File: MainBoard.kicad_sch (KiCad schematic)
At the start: 85 parts, among them J1 Conn_01x04, J10 Conn_01x02, J11 Conn_01x03, J12 Conn_01x03, J13 Conn_01x04, J14 Conn_01x03, J15 Conn_01x04, J16 Conn_01x05, J17 Conn_01x05, J18 Conn_01x06, J19 Conn_01x05, J2 Conn_01x04, J20 Conn_01x08, J21 Conn_01x03, J22 Conn_01x03, J23 Conn_01x05, J24 Conn_01x04, J25 Conn_01x04, J26 Conn_01x04, J27 Conn_01x04, J28 Conn_01x04, J3 Conn_01x06, J4 Conn_01x02, J5 Conn_01x02, J6 Conn_01x02, J7 Conn_01x04, J8 Conn_01x04, J9 Conn_01x02, Q1 NMOS_80A, Q10 NMOS_80A, Q11 NMOS_80A, Q12 NMOS, Q2 NMOS_80A, Q3 NMOS_80A, Q4 NMOS, Q5 NMOS, Q6 NMOS, Q7 NMOS, Q8 NMOS, Q9 NMOS, U1 TJA1051T-3, U10 INA228, U2 INA228, U5 INA228, U6 ESP32-DEVKITC-32D, U7 MCP23017_SO, U8 MCP23017_SO, U9 INA228

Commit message: test
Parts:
- removed C1, C2, C3, C4, C5, C6: 100nF, Capacitor_SMD:C_1206_3216Metric_Pad1.33x1.80mm_HandSolder, symbol Device:C
- removed D1, D2, D3, D4, D8, D9: US1M, Diode_SMD:D_SMA, symbol Diode:US1M
- removed D10, D11, D5, D6, D7: WS2812B, LED_SMD:LED_WS2812B_PLCC4_5.0x5.0mm_P3.2mm, symbol LED:WS2812B
- removed J1, J13, J15, J2, J24, J25, J26, J27, J28, J7, J8: Conn_01x04, velion_mainboard:15EDG-4P, symbol Connector_Generic:Conn_01x04
- removed J10, J4, J5, J6, J9: Conn_01x02, velion_mainboard:15EDG-2P, symbol Connector_Generic:Conn_01x02
- removed J11, J12, J14, J21, J22: Conn_01x03, velion_mainboard:15EDG-3P, symbol Connector_Generic:Conn_01x03
- removed J16, J17, J19, J23: Conn_01x05, velion_mainboard:15EDG-5P, symbol Connector_Generic:Conn_01x05
- removed J18, J3: Conn_01x06, velion_mainboard:15EDG-6P, symbol Connector_Generic:Conn_01x06
- removed J20: Conn_01x08, velion_mainboard:GY-91, symbol Connector_Generic:Conn_01x08
- removed Q1, Q10, Q11, Q2, Q3: NMOS_80A, velion_mainboard:NMOS_80A, symbol Transistor_FET_Other:Q_NMOS_Depletion_GDS
- removed Q12, Q4, Q5, Q6, Q7, Q8, Q9: NMOS, Package_TO_SOT_SMD:SOT-23, symbol Transistor_FET_Other:Q_NMOS_Depletion_GSD
- removed R1, R2, R8, R9: 0.001 R, Resistor_SMD:R_2512_6332Metric_Pad1.40x3.35mm_HandSolder, symbol Device:R
- removed R10, R12, R13, R14, R15, R16: 100 R, Resistor_SMD:R_1206_3216Metric_Pad1.30x1.75mm_HandSolder, symbol Device:R
- removed R11, R17: 10 K, Resistor_SMD:R_1206_3216Metric_Pad1.30x1.75mm_HandSolder, symbol Device:R
- removed R18: 120 R, Resistor_SMD:R_1206_3216Metric_Pad1.30x1.75mm_HandSolder, symbol Device:R
- removed R3, R4, R5: 100R, Resistor_SMD:R_1206_3216Metric_Pad1.30x1.75mm_HandSolder, symbol Device:R
- removed R6, R7: 4k7, Resistor_SMD:R_1206_3216Metric_Pad1.30x1.75mm_HandSolder, symbol Device:R
- removed U1: TJA1051T-3, Package_SO:SOIC-8_3.9x4.9mm_P1.27mm, symbol Interface_CAN_LIN:TJA1051T-3
- removed U10, U2, U5, U9: INA228, Package_SO:VSSOP-10_3x3mm_P0.5mm, symbol Sensor_Energy:INA228
- removed U3: ~, velion_mainboard:BUCK5V, symbol velion_mainboard:buck5V
- removed U4: ~, velion_mainboard:BUCK12V, symbol velion_mainboard:buck12V
- removed U6: ESP32-DEVKITC-32D, velion_mainboard:MODULE_ESP32-DEVKITC-32D, symbol ESP32-DEVKITC-32D:ESP32-DEVKITC-32D
- removed U7, U8: MCP23017_SO, Package_SO:SOIC-28W_7.5x17.9mm_P1.27mm, symbol Interface_Expansion:MCP23017_SO
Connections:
- no-connect marks 22 -> 0
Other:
- note added: "test"
- note removed: "(3V3-2V)/10 mA=100 R"
- note removed: "+ - -"
- note removed: "0100000 = 0x20"
- note removed: "0100001 = 0x21"
- note removed: "1 mosfet 40 A 1 mosfet 10 A 9 mosfet 5 A 1 current sensing 40 A 1 current sensing 10 A 4 current sensing 5 A 9 IO for 3 rotatary encoder (A/B + button) 2 IO for PAS 1 IO for Speed Input 2 IO brake sensor switch 1 IO seat sensor switch 1 IO trunk latch switch 5 IO LED 2 IO reverse selector 1 IO defrost button 1 IO cabin light button 1 IO warning button 1 IO brouillard button 1 IO WS2812"
- note removed: "1-2 CHF N-channel 100V 0.012 Ohm 80A"
- note removed: "1000000 -> 0x40"
- note removed: "1000001 -> 0x41"
- note removed: "1000100 -> 0x44"
- note removed: "1000101 -> 0x45"
- note removed: "10A"
- note removed: "10A Fuse here"
- note removed: "2A MAX"
- note removed: "2A max"
- note removed: "35-60V"
- note removed: "3v3 provided by internal LDO of ESP32 devboard"
- note removed: "40A Fuse Here"
- note removed: "40A Fuse here"
- note removed: "5 V"
- note removed: "5-12 V"
- note removed: "5A MAX"
- note removed: "AUX Power distribution"
- note removed: "AUX USB-C"
- note removed: "AUX audio"
- note removed: "Blinker + Trunk Latch + Int light"
- note removed: "Brouillard button + led"
- note removed: "Buttons Dashboard"
- note removed: "CAN BUS Power Rail"
- note removed: "CAN Display"
- note removed: "CAN Front"
- note removed: "CAN Handle"
- note removed: "CAN REAR"
- note removed: "CAN Transceiver"
- note removed: "CabinLighting button + led"
- note removed: "Compute"
- note removed: "Defrost button + led"
- note removed: "Defroster"
- note removed: "Defroster Driver"
- note removed: "EncoderHandHeater"
- note removed: "EncoderSeatHeater"
- note removed: "EncoderSpeedLimit"
- note removed: "Fuse"
- note removed: "Handle Heater + Brake Sensor"
- note removed: "IMU 10 DOF"
- note removed: "Latch Trunk Interrior Lightning"
- note removed: "Latch Trunk button + led"
- note removed: "MPU9250 : 1101000 -> 0x68 BMP280 : 1110110 -> 0x76"
- note removed: "Mapping button + led"
- note removed: "Never powered Down so that emergency signal keep blinking"
- note removed: "Never powered Down so that soft power button keep working"
- note removed: "PAS"
- note removed: "PAS + Throttle INPUT"
- note removed: "POWER is a signal to power on / off (using rising / falling edge) the siliXcon controller."
- note removed: "Power Input"
- note removed: "Protect all CAN Bus"
- note removed: "RGB backlight"
- note removed: "Rear-view left (LED + blinker)"
- note removed: "Rear-view right (LED + blinker)"
- note removed: "Reverse button"
- note removed: "Rotary Encoder Dashboard"
- note removed: "Seat + Hand Warmer Brake + seat sensor"
- note removed: "Seat Heater + Seat Sensor"
- note removed: "Solar Pannel MPPT"
- note removed: "Speed input"
- note removed: "The Fuse are wired externally from the PCB"
- note removed: "Use MCP internal pullups"
- note removed: "VIN 3V3 GND SCL SDA SDG/SA0 NCS CSB"
- note removed: "Warning button + led"
- note removed: "XT60 2+4 Power IN + CAN + KEY"
- note removed: "diode -> little hack to drive the WS2812 using 3v3 logic"
- note removed: "either one or none can be pulled LOW, but not both -> Fault condition"
- note removed: "https://de.aliexpress.com/item/1005008076581555.html GY-91 MPU-9250 and BMP280 10 DOF"
- note removed: "https://hackaday.com/2017/01/20/cheating-at-5v-ws2812-control-to-use-a-3-3v-data-line/"
- note removed: "leave serial port for debug"
- note removed: "resistor to limit risk of issue due to current leakage and the mosfet grid capacitor that could influence the strapping pin at boot."
- note removed: "small sig 20 V 5A mosfet"
- note removed: "to make assembly easier, we use encoder with PCB that aldready have the pullup and everything"
- note removed: "untouched, for MPU9250 SPI mode"
- note removed: "untouched, internal LDO"
- note removed: "untouched, to change MPU9250 I2C address"
- note removed: "untouched, used to set BMP to SPI mode"
- note removed: "use pullup"

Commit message: better
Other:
- note added: "test2"
- note removed: "test"
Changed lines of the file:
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@@
 	(generator_version "10.0")
 	(paper "A3")
-	(text "test"
+	(text "test2"
 		(exclude_from_sim no)
 		(at 148.844 113.284 0)

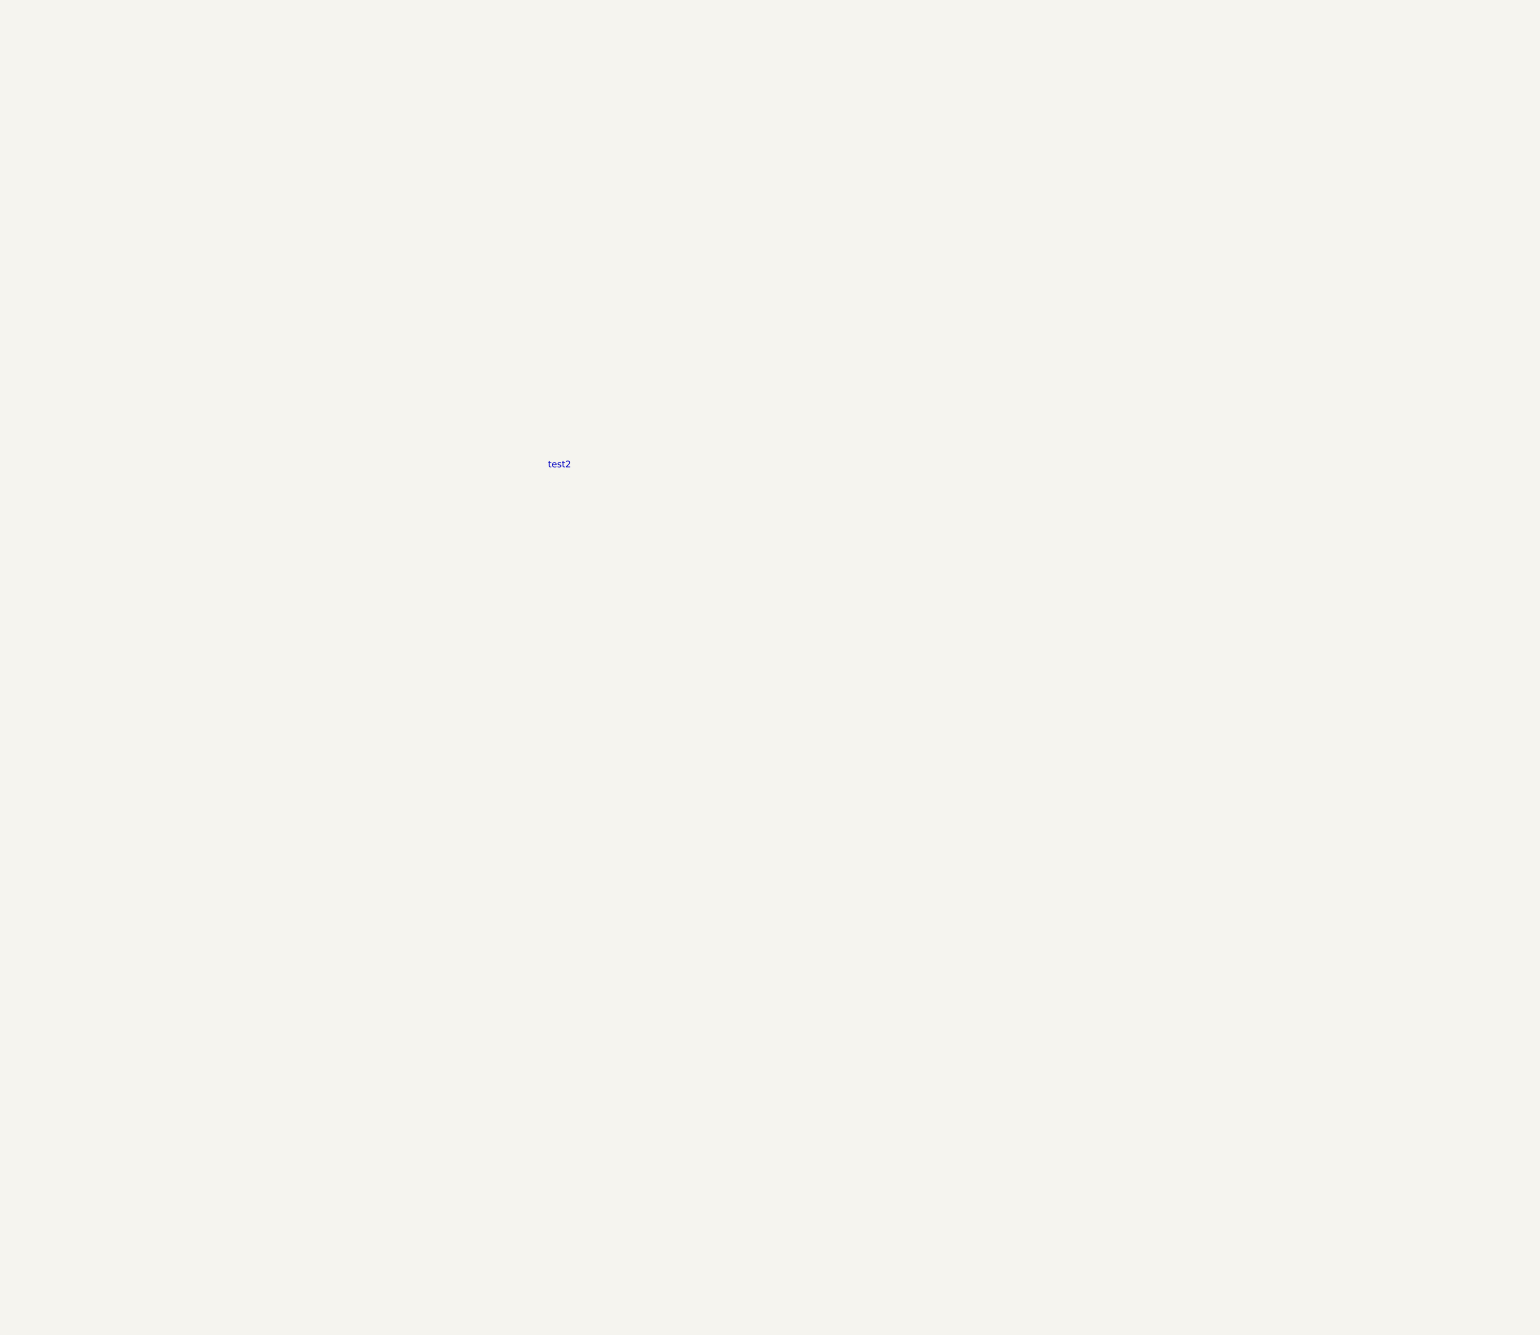
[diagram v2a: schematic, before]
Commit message: Block division draft + mounting holes and assembly fiducials
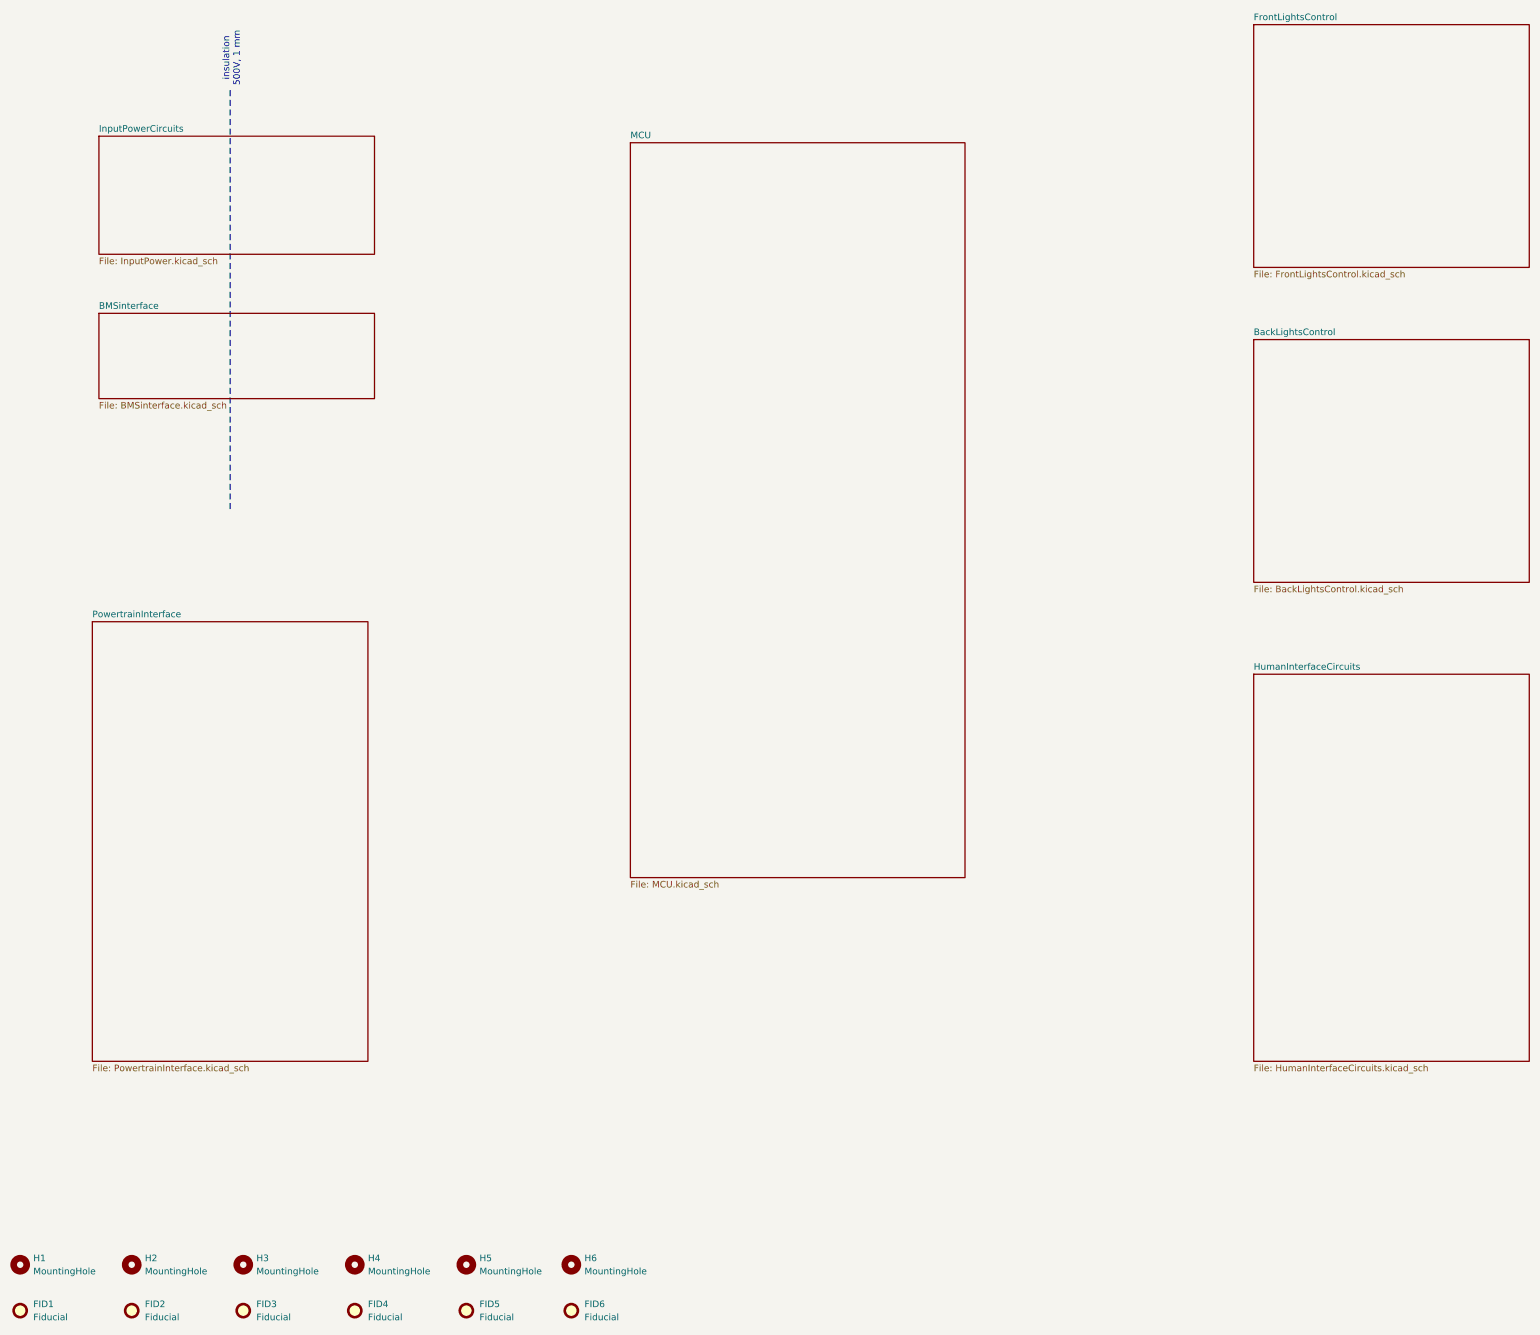
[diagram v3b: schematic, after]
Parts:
- added FID1, FID2, FID3, FID4, FID5, FID6: Fiducial, Fiducial:Fiducial_1mm_Mask2mm, symbol Mechanical:Fiducial
- added H1, H2, H3, H4, H5, H6: MountingHole, MountingHole:MountingHole_3.2mm_M3, symbol Mechanical:MountingHole
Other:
- added sheet BMSinterface (BMSinterface.kicad_sch)
- added sheet BackLightsControl (BackLightsControl.kicad_sch)
- added sheet FrontLightsControl (FrontLightsControl.kicad_sch)
- added sheet HumanInterfaceCircuits (HumanInterfaceCircuits.kicad_sch)
- added sheet InputPowerCircuits (InputPower.kicad_sch)
- added sheet MCU (MCU.kicad_sch)
- added sheet PowertrainInterface (PowertrainInterface.kicad_sch)
- note added: "insulation 500V, 1 mm"
- note removed: "test2"
